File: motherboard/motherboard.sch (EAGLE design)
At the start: 55 parts, among them IC1 USB6B1, Q1 MOSFET-NCHANNELPTH2, T1 2N3904, T2 2N3904, U1 LED_100V_BUCK, U2 LED_100V_BUCK, U3 LED_100V_BUCK, U4 LED_100V_BUCK, X1 USB_3P-85-32003-00X-1

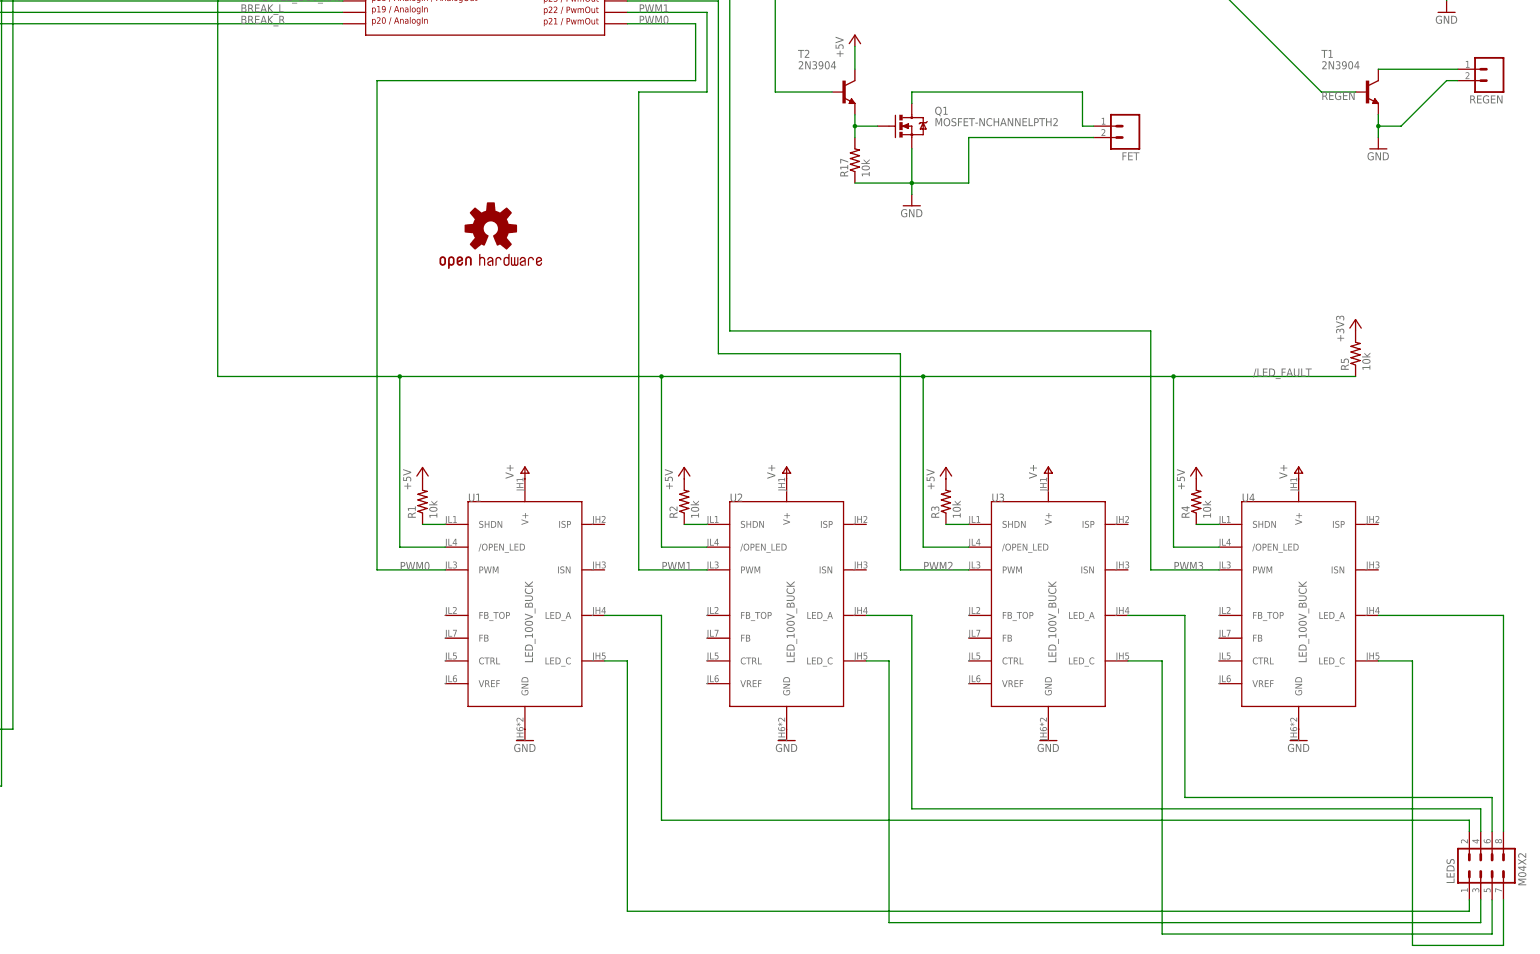
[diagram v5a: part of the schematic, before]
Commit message: Add under voltage cutoff to LED drivers
Add exports of the motherboard schematic.
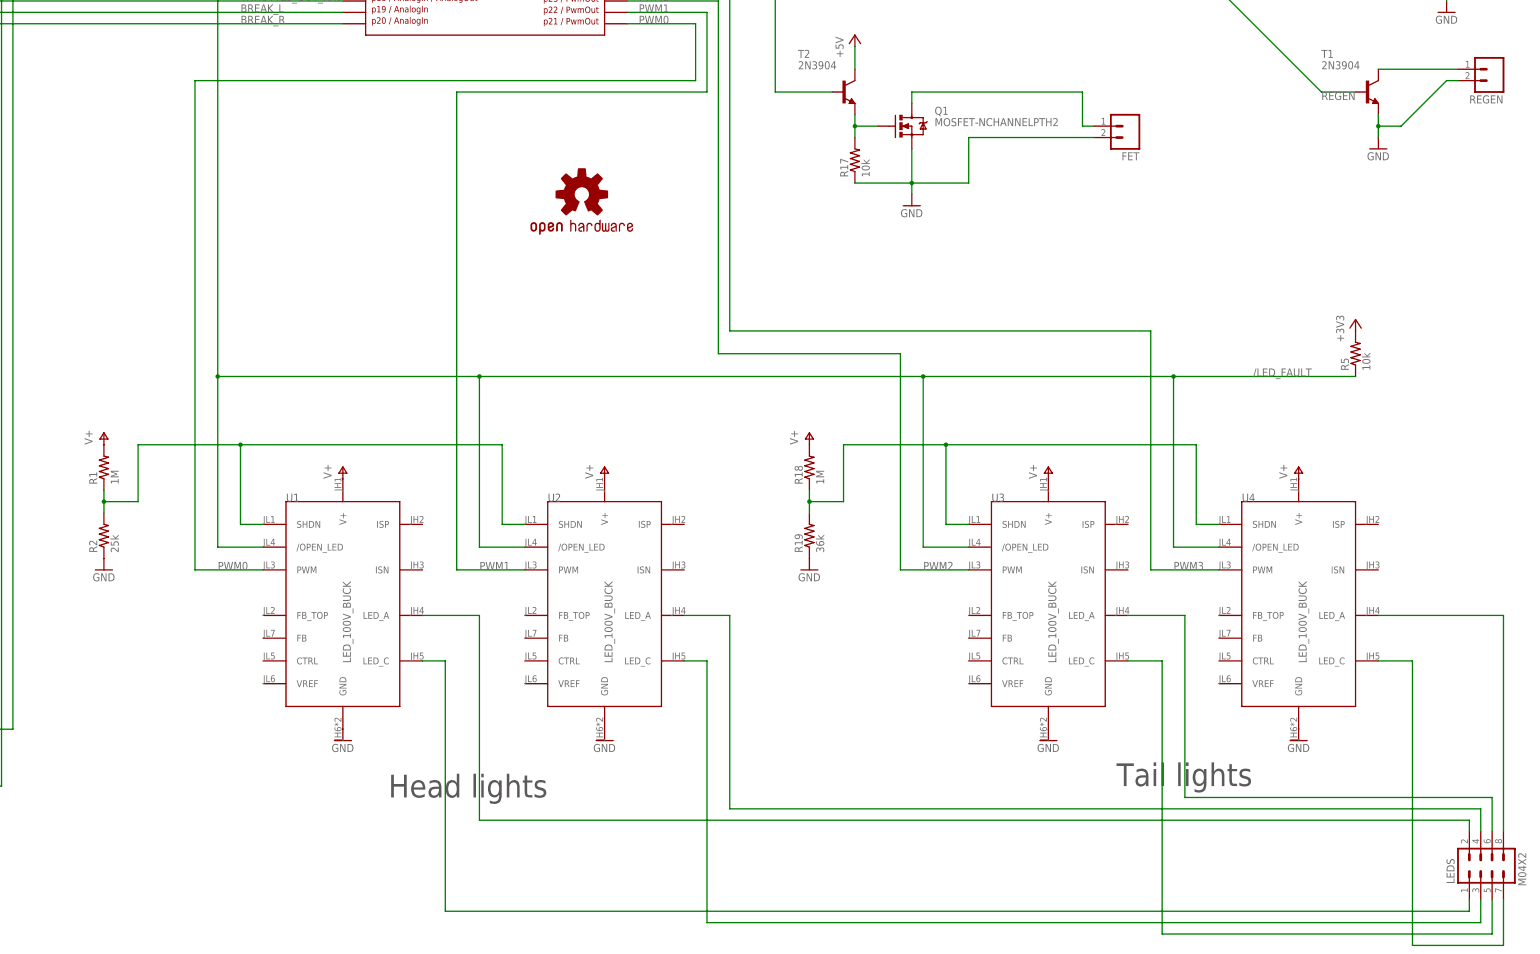
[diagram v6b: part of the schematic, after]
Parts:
- removed R3, R4: 10k, rcl:R-US_0204/5
- added R18: 1M, rcl:R-US_0204/5
- added R19: 36k, rcl:R-US_0204/5
- R1: value 10k -> 1M
- R2: value 10k -> 25k
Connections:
- removed net N$12: R4.1, U4.SHDN
- removed net N$13: R2.1, U2.SHDN
- net +5V: no longer R1.2, R2.2, R3.2, R4.2
- net GND: now also R19.1, R2.1
- net N$10: now also R2.2, U2.SHDN
- net N$11: now also R18.1, R19.2, U4.SHDN; no longer R3.1
- net V+: now also R1.2, R18.2
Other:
- note added: "Head lights"
- note added: "Tail lights"
- moved on the sheet: R1, R2, U1, U2

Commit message: Add LTC2990 current and voltage monitoring chip
Still needs to be connected.
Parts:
- removed C1, C2: (no value), rcl:C-US050-024X044
- removed D2: 3.3V, SparkFun-DiscreteSemi:DIODE-ZENERPTH
- removed PTC3: (no value), ptc-ntc:PTC679
- removed R8: 100k, SparkFun-Electromechanical:TRIMPOT3362U-2
- added U$3: LTC2990, droidcycle:LTC2990
- R13, R14: value 1k -> 10k
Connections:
- removed net MOT_CUR: D2.C, OA1G$1.OUT, R8.CW, U$1.P$15
- removed net N$21: F1.2, R11.1
- removed net N$22: C2.1, PHOTO.2, R13.2
- removed net N$23: C1.1, PHOTO.4, R14.2
- removed net N$27: PTC3.2, X1B.1
- new net N$12: R6.1
- new net N$13: IC1.IO1, X1A.2
- net +3V3: now also R13.1, R14.1
- net +5V: now also IC1.VCC; no longer OA1G$1.V+, PTC3.1
- net BATT_SENSE: no longer U$1.P$16
- net CADENCE: now also U$1.P$8
- net GND: now also IC1.GND; no longer C1.2, C2.2, D2.A, OA1G$1.V-, X1B.4
- net N$16: now also IC1.IO2, X1A.3; no longer OA1G$1.-IN, R6.1, R8.WIPER
- net N$17: no longer OA1G$1.+IN
- net PHOTO1: now also PHOTO.4, R14.2, U$1.P$15; no longer R14.1
- net PHOTO2: now also PHOTO.2, R13.2, U$1.P$16; no longer R13.1
- net SPEED: now also U$1.P$7
- net V+: now also F1.2, R11.1
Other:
- moved on the sheet: PTC2, R13, R14, X1A

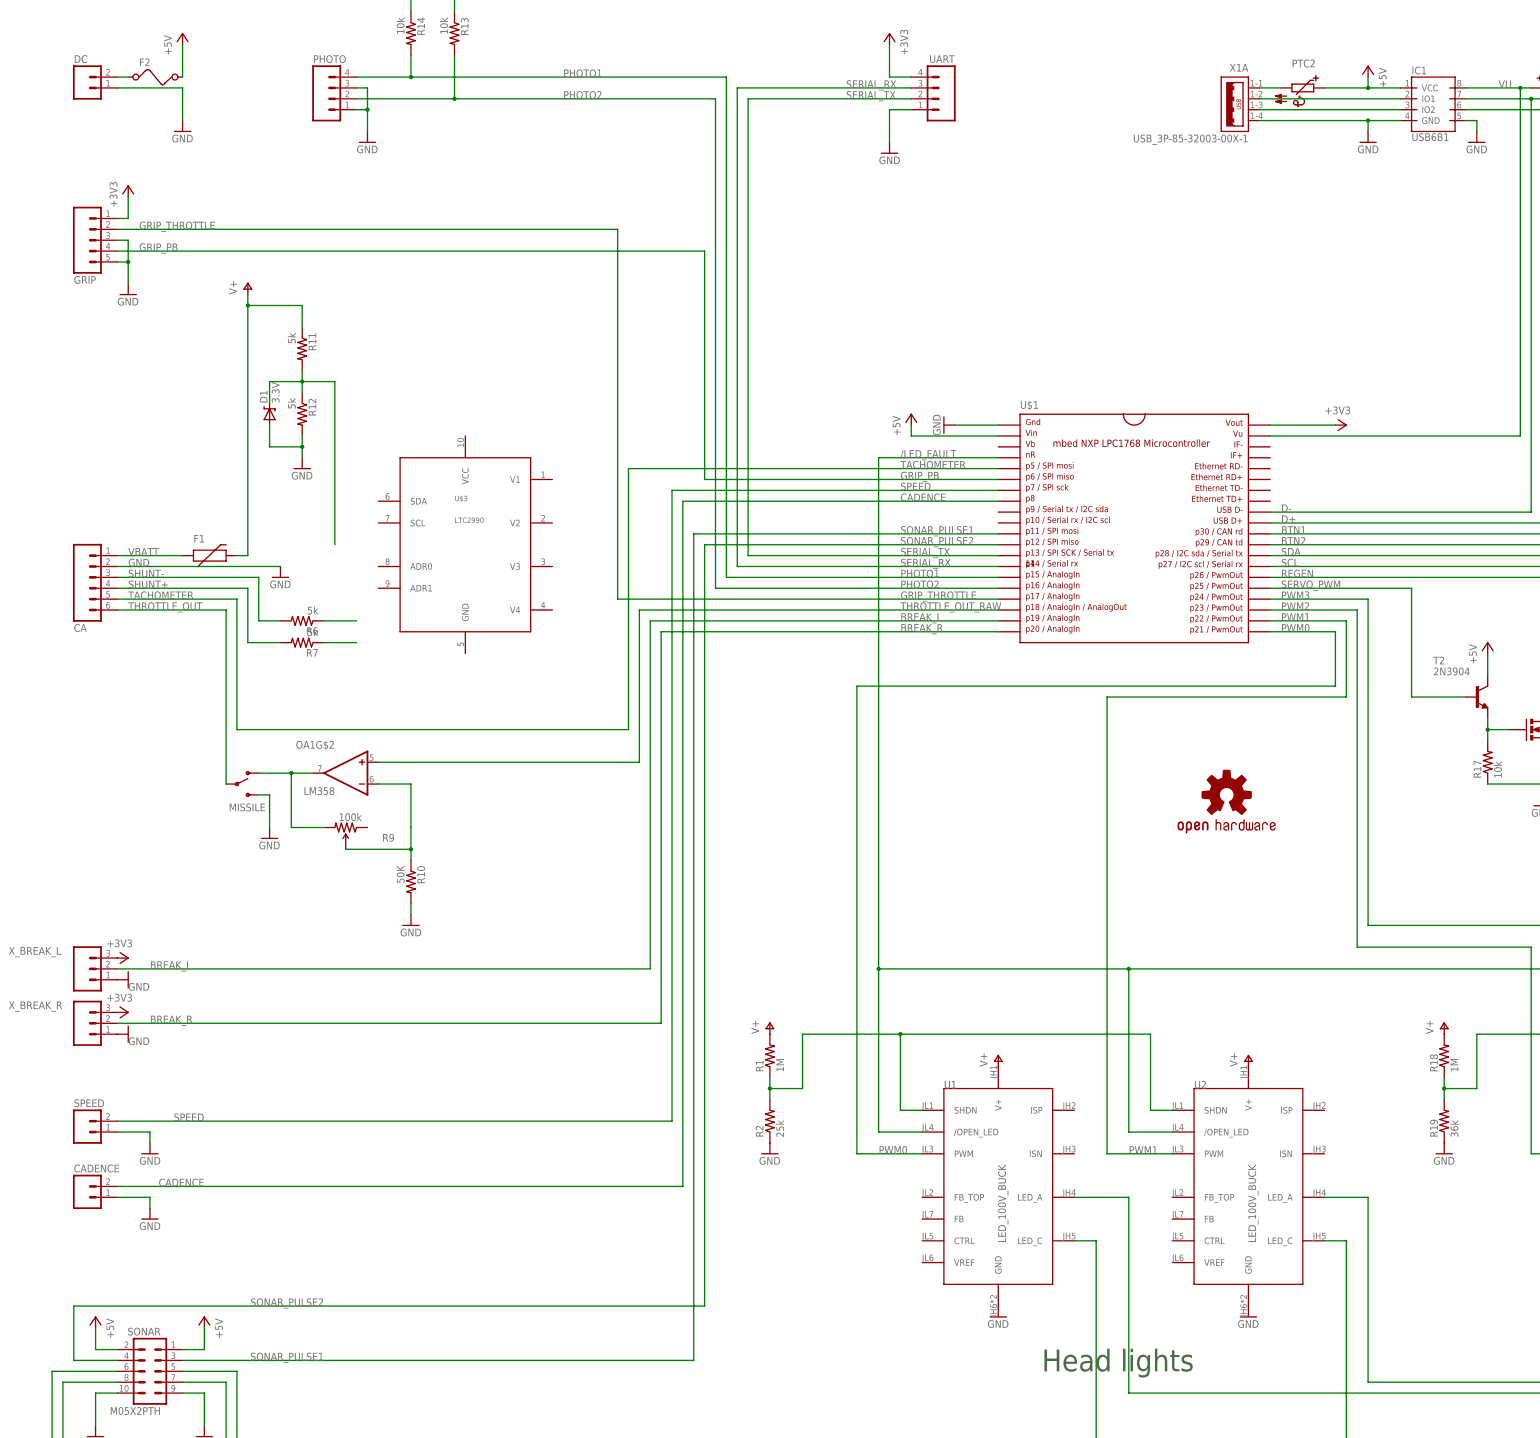
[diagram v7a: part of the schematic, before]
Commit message: Finish adding voltage monitoring IC.
Generate bill of materials.
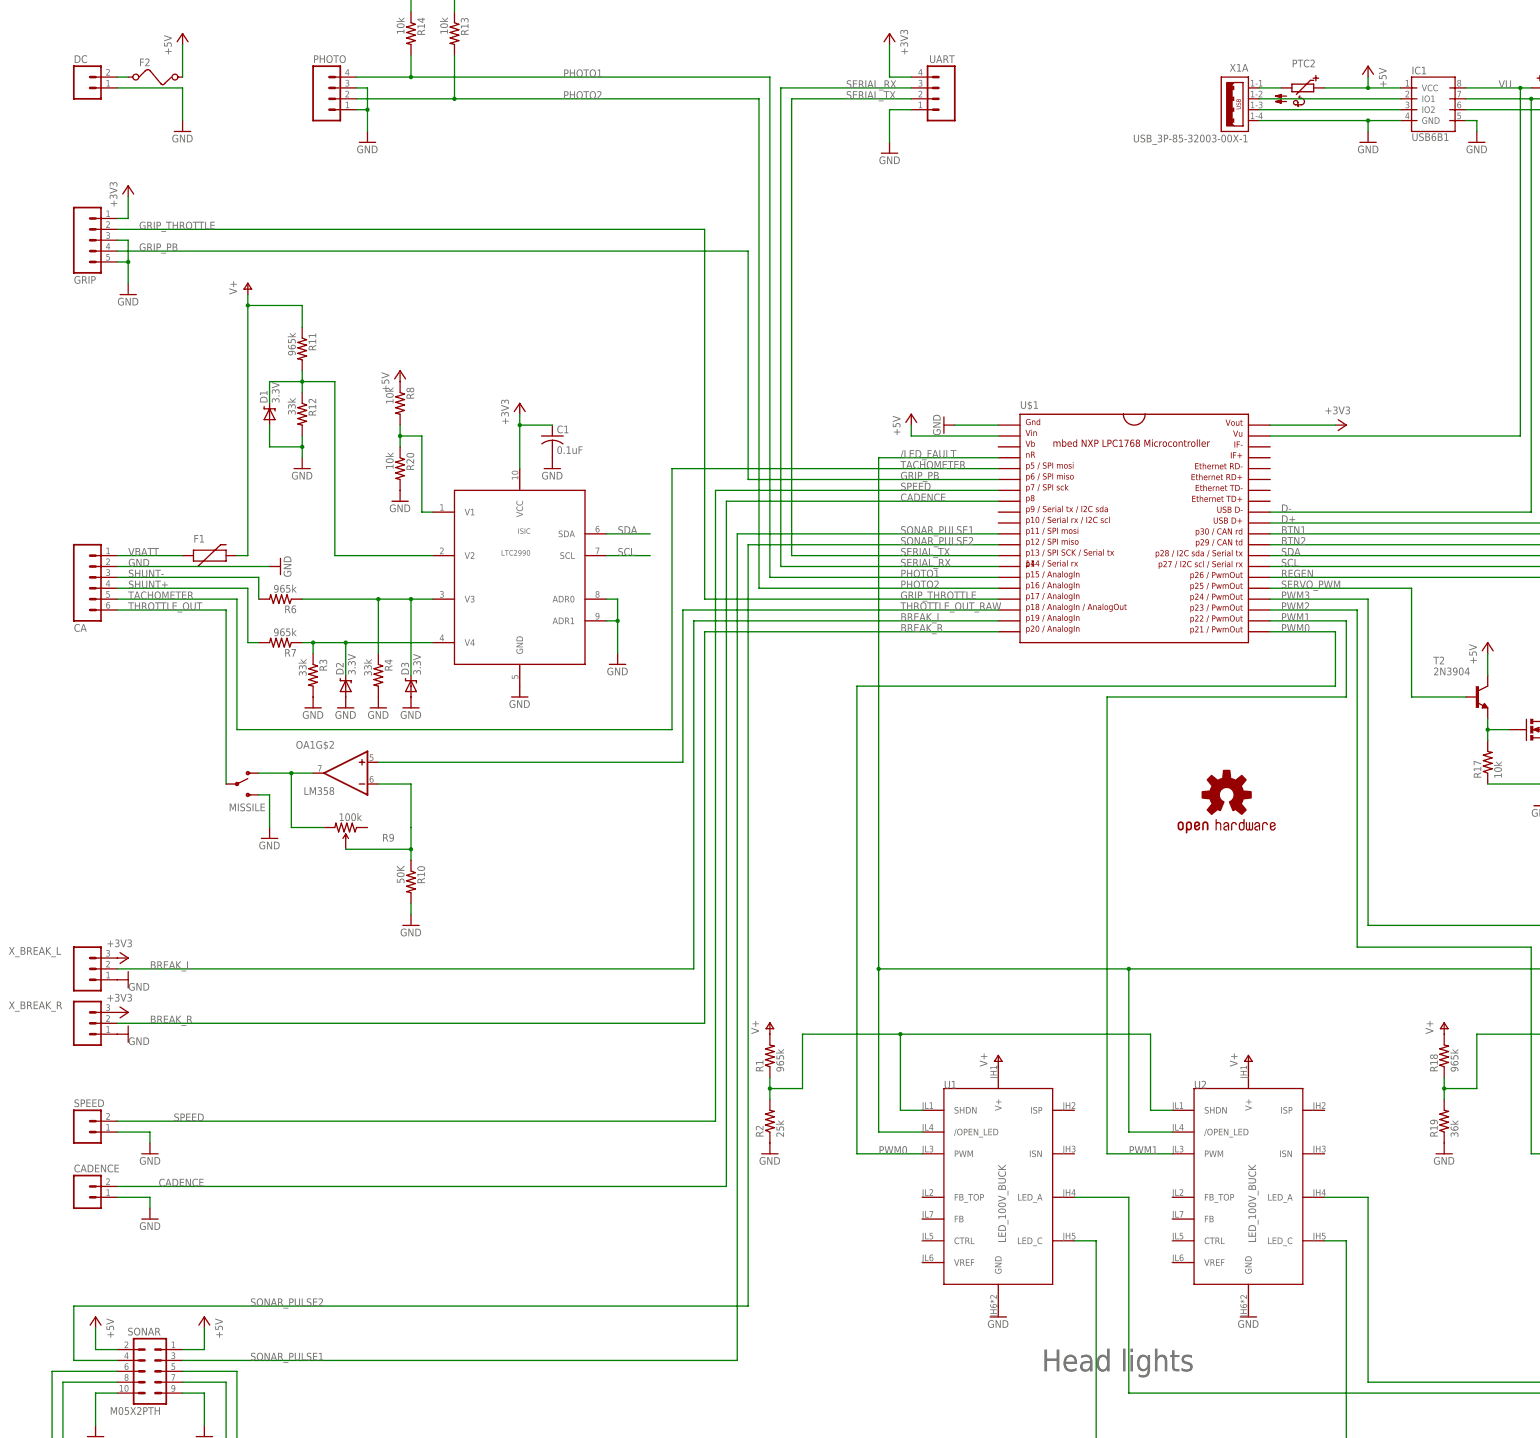
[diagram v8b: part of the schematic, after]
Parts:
- removed U$3: LTC2990, droidcycle:LTC2990
- added C1: 0.1uF, rcl:C-US050-025X075
- added D2, D3: 3.3V, SparkFun-DiscreteSemi:DIODE-ZENERPTH
- added ISIC: LTC2990, droidcycle:LTC2990
- added R20, R8: 10k, rcl:R-US_0204/5
- added R3, R4: 33k, rcl:R-US_0204/5
- R1, R18: value 1M -> 965k
- R11, R6, R7: value 5k -> 965k
- R12: value 5k -> 33k
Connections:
- new net N$21: ISIC.V1, R20.1, R8.2
- net +3V3: now also C1.1, ISIC.VCC
- net +5V: now also R8.1
- net BATT_SENSE: now also ISIC.V2
- net GND: now also C1.2, D2.A, D3.A, ISIC.ADR0, ISIC.ADR1, ISIC.GND, R20.2, R3.2, R4.2
- net N$12: now also D3.C, ISIC.V3, R4.1
- net N$17: now also D2.C, ISIC.V4, R3.1
- net SCL: now also ISIC.SCL
- net SDA: now also ISIC.SDA
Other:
- moved on the sheet: R6, R7
